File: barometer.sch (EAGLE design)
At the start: 103 parts, among them IC1 TPS5410, IC2 ZPA2326-0311A-R, IC3 MIC5225-3.3v, Q1 BC817, U1 LTC2850, U2 PCA9306, U3 DAC8574, U4 XTR117, U5 XC6215XC6215B182NR, U6 MAX3221, U7 Tiny85-20-SMT, X1 1751248, X2 1751264

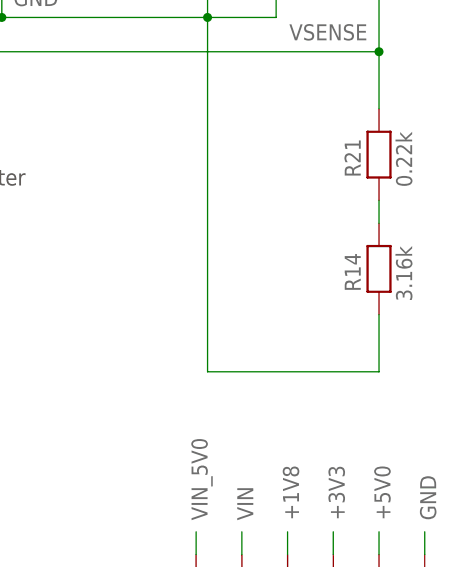
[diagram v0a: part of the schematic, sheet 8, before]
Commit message: Fix feedback resistance in +5V0 buck converter
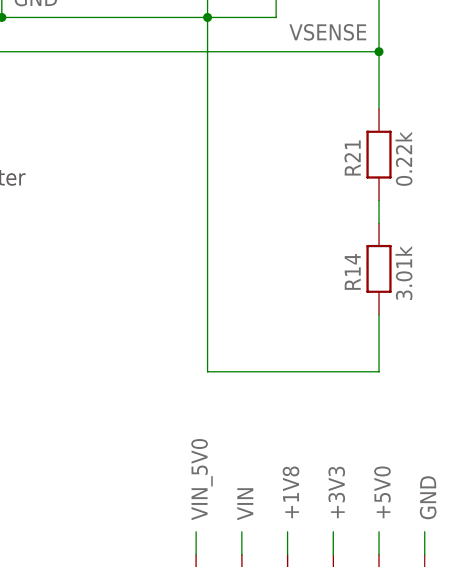
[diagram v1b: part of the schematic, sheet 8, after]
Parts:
- R14: value 3.16k -> 3.01k
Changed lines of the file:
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@@
 <part name="L1" library="inductor-tdk" deviceset="INDUCTOR-TDK" device="VLS6045EX" value="68u"/>
 <part name="R10" library="microbuilder" deviceset="RESISTOR" device="0603" value="10k"/>
-<part name="R14" library="microbuilder" deviceset="RESISTOR" device="0603" value="3.16k"/>
+<part name="R14" library="microbuilder" deviceset="RESISTOR" device="0603" value="3.01k"/>
 <part name="IC2" library="barometer-murata" deviceset="ZPA2326" device="-0311A-R"/>
 <part name="R19" library="microbuilder" deviceset="RESISTOR" device="0603" value="1k"/>

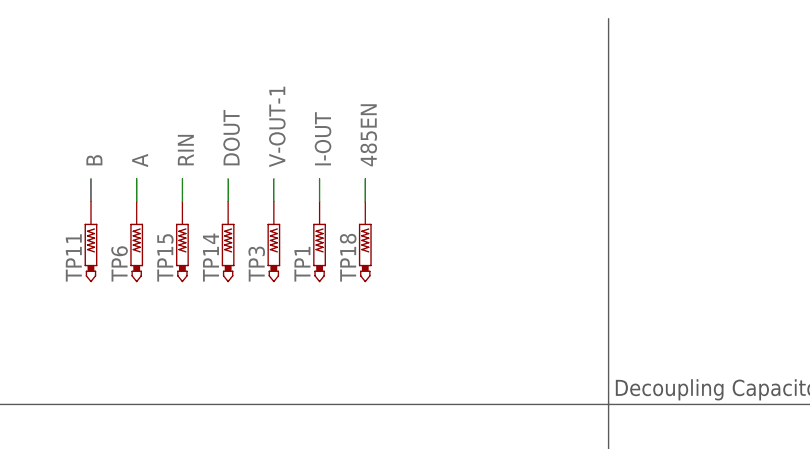
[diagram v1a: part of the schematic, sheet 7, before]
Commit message: Add test point for DAC output corresponding to 4-20 mA current loop
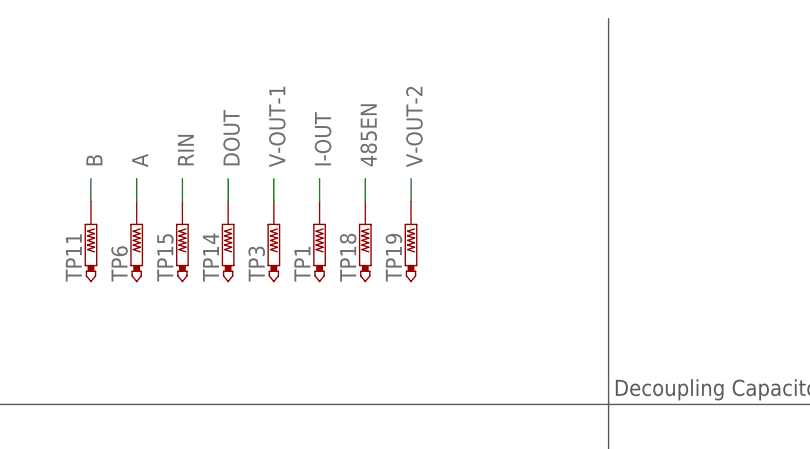
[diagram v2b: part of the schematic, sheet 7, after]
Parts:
- added TP19: PTR1B1,27, testpad:PTR1B1,27
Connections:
- net V-OUT-2: now also TP19.TP
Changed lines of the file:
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@@
 <part name="C19" library="microbuilder" deviceset="CAP_CERAMIC" device="0603" value="0.1u"/>
 <part name="C20" library="microbuilder" deviceset="CAP_CERAMIC" device="0603" value="0.1u"/>
+<part name="TP19" library="testpad" library_urn="urn:adsk.eagle:library:385" deviceset="PTR1" device="B1,27" package3d_urn="urn:adsk.eagle:package:27944/1"/>
 </parts>
 <sheets>
@@
 <attribute name="VALUE" x="143.51" y="152.4" size="1.778" layer="96" font="vector"/>
 </instance>
+<instance part="TP19" gate="G$1" x="66.04" y="152.4" smashed="yes">
+<attribute name="NAME" x="65.024" y="146.05" size="1.778" layer="95" font="vector" rot="R90"/>
+<attribute name="TP_SIGNAL_NAME" x="67.31" y="149.86" size="1.778" layer="97"/>
+</instance>
 </instances>
 <busses>
@@
 <label x="189.865" y="73.66" size="1.778" layer="95" font="vector" rot="R180"/>
 </segment>
-</net>
+<segment>
+<pinref part="TP19" gate="G$1" pin="TP"/>
+<wire x1="66.04" y1="154.94" x2="66.04" y2="157.48" width="0.1524" layer="91"/>
+<label x="67.31" y="158.75" size="1.778" layer="95" font="vector" rot="R90"/>
+</segment>
+</net>

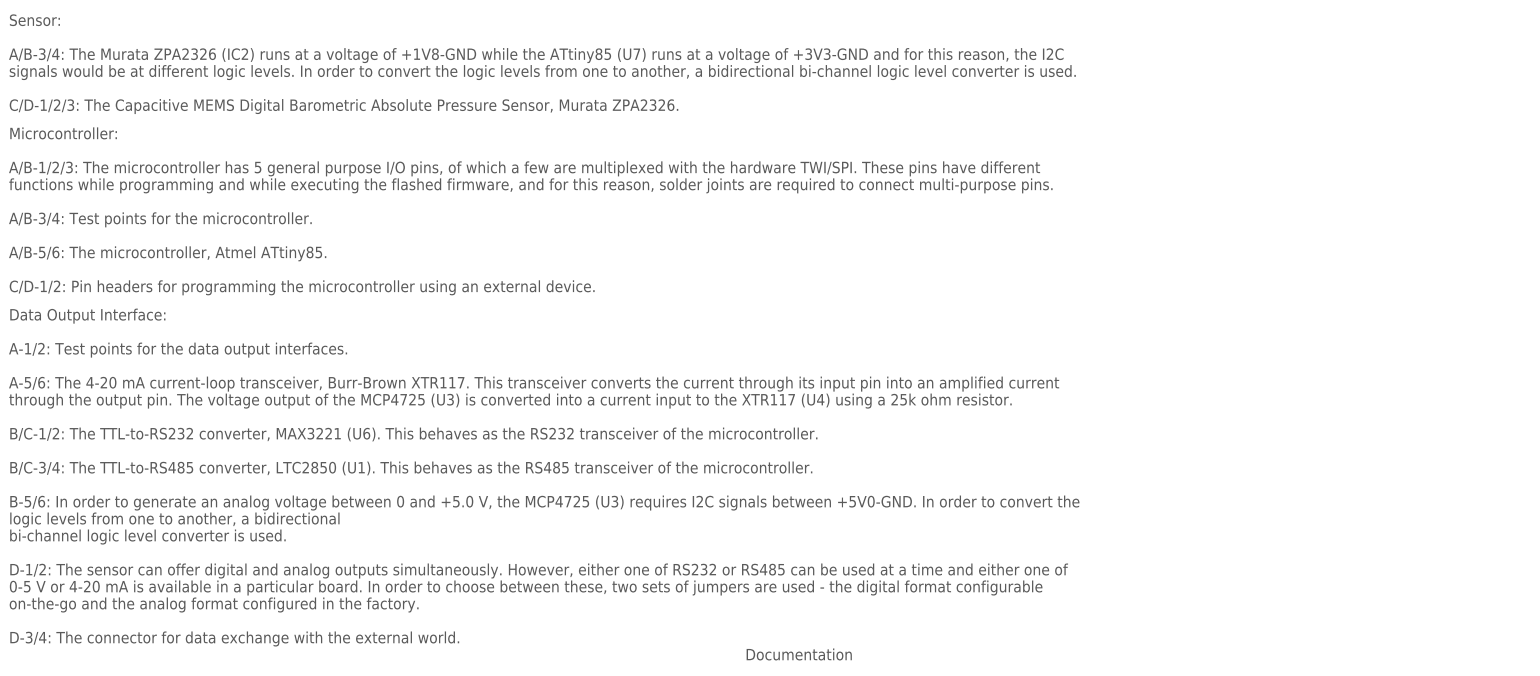
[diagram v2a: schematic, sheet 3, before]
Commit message: Fix schematic documentation
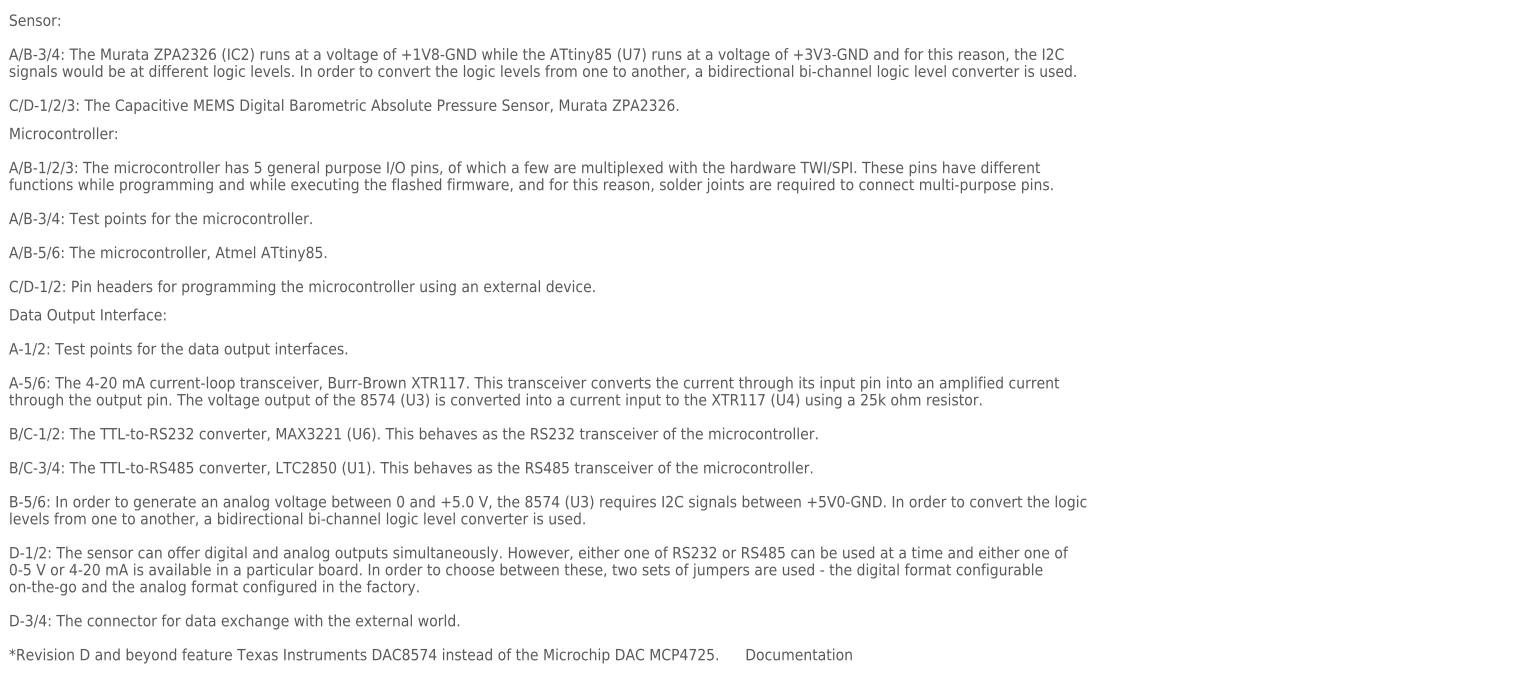
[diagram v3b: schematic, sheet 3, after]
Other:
- note added: "Data Output Interface: A-1/2: Test points for the data output interfaces. A-5/6: The 4-20 mA current-loop transceiver, Burr-Brown XTR117. This transceiver converts the current through its input pin into an amplified current through the output pin. The voltage output of the 8574 (U3) is converted into a current input to the XTR117 (U4) using a 25k ohm resistor. B/C-1/2: The TTL-to-RS232 converter,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"
- note added: "Digital to Analog Converter for 0-5 V terminals 8574"
- note removed: "Data Output Interface: A-1/2: Test points for the data output interfaces. A-5/6: The 4-20 mA current-loop transceiver, Burr-Brown XTR117. This transceiver converts the current through its input pin into an amplified current through the output pin. The voltage output of the MCP4725 (U3) is converted into a current input to the XTR117 (U4) using a 25k ohm resistor. B/C-1/2: The TTL-to-RS232 convert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"
- note removed: "Digital to Analog Converter for 0-5 V terminals MCP4725"
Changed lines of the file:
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@@
 <text x="50.8" y="99.06" size="2.54" layer="97" font="vector" align="center">Digital to Analog Converter
 for 0-5 V terminals
-MCP4725</text>
+8574</text>
 <text x="147.32" y="73.66" size="2.54" layer="97" font="vector" align="center">TTL to RS-232/RS-485
 Transceivers
@@
 A-1/2: Test points for the data output interfaces.
 A-5/6: The 4-20 mA current-loop transceiver, Burr-Brown XTR117. This transceiver converts the current through its input pin into an amplified current
-through the output pin. The voltage output of the MCP4725 (U3) is converted into a current input to the XTR117 (U4) using a 25k ohm resistor.
+through the output pin. The voltage output of the 8574 (U3) is converted into a current input to the XTR117 (U4) using a 25k ohm resistor.
 B/C-1/2: The TTL-to-RS232 converter, MAX3221 (U6). This behaves as the RS232 transceiver of the microcontroller.
 B/C-3/4: The TTL-to-RS485 converter, LTC2850 (U1). This behaves as the RS485 transceiver of the microcontroller.
-B-5/6: In order to generate an analog voltage between 0 and +5.0 V, the MCP4725 (U3) requires I2C signals between +5V0-GND. In order to convert the
-logic levels from one to another, a bidirectional
-bi-channel logic level converter is used.
+B-5/6: In order to generate an analog voltage between 0 and +5.0 V, the 8574 (U3) requires I2C signals between +5V0-GND. In order to convert the logic
+levels from one to another, a bidirectional bi-channel logic level converter is used.
 D-1/2: The sensor can offer digital and analog outputs simultaneously. However, either one of RS232 or RS485 can be used at a time and either one of
 0-5 V or 4-20 mA is available in a particular board. In order to choose between these, two sets of jumpers are used - the digital format configurable
 on-the-go and the analog format configured in the factory.
-D-3/4: The connector for data exchange with the external world.</text>
+D-3/4: The connector for data exchange with the external world.
+*Revision D and beyond feature Texas Instruments DAC8574 instead of the Microchip DAC MCP4725.</text>
 </plain>
 <instances>

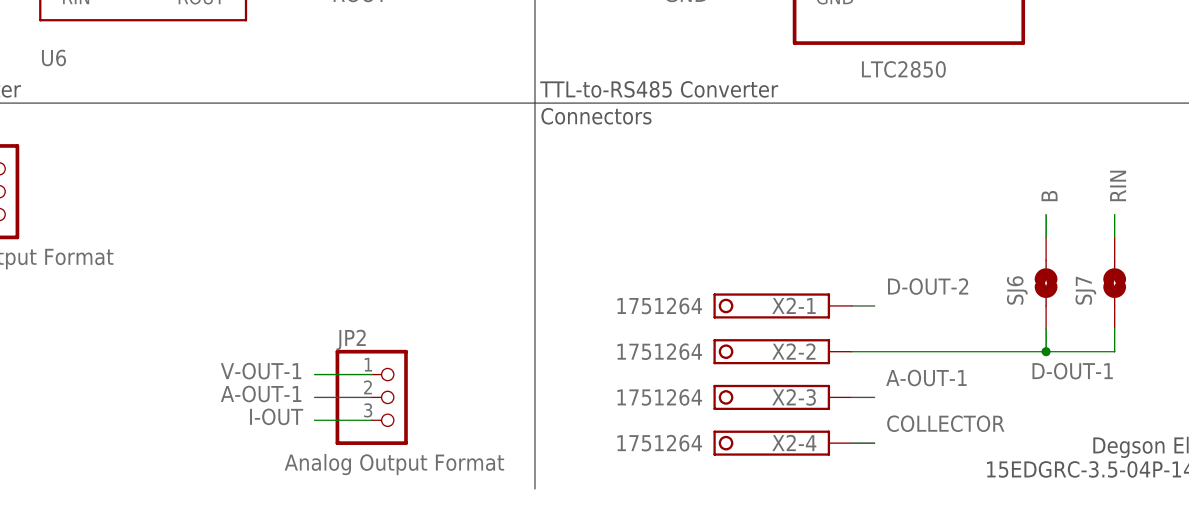
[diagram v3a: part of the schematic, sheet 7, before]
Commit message: Add additional jumper for analog output format
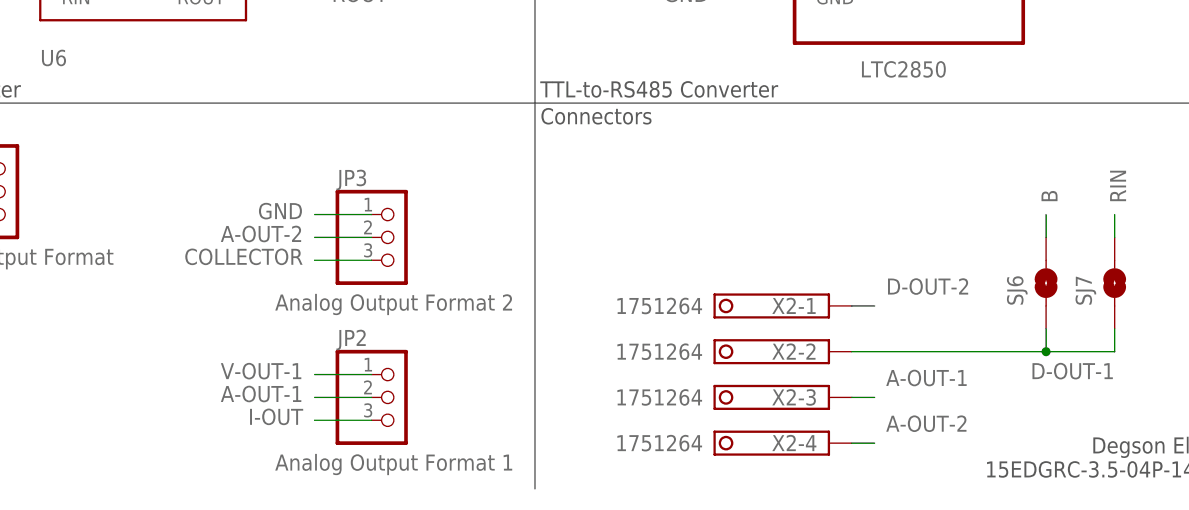
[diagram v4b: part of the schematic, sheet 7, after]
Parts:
- added JP3: Analog Output Format 2, microbuilder:HEADER-1X3SMT
- JP2: value Analog Output Format -> Analog Output Format 1
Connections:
- new net A-OUT-2: JP3.2, X2-4.K
- net COLLECTOR: now also JP3.3; no longer X2-4.K
- net GND: now also JP3.1
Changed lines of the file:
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@@
 <part name="FRAME9" library="microbuilder" deviceset="FRAME_A4_WEATHER" device=""/>
 <part name="R21" library="microbuilder" deviceset="RESISTOR" device="0603" value="0.22k"/>
-<part name="JP2" library="microbuilder" deviceset="HEADER-1X3" device="SMT" value="Analog Output Format"/>
+<part name="JP2" library="microbuilder" deviceset="HEADER-1X3" device="SMT" value="Analog Output Format 1"/>
 <part name="U3" library="texas-msp" deviceset="DAC8574" device=""/>
 <part name="C18" library="microbuilder" deviceset="CAP_CERAMIC" device="0603" value="0.1u"/>
@@
 <part name="C20" library="microbuilder" deviceset="CAP_CERAMIC" device="0603" value="0.1u"/>
 <part name="TP19" library="testpad" library_urn="urn:adsk.eagle:library:385" deviceset="PTR1" device="B1,27" package3d_urn="urn:adsk.eagle:package:27944/1"/>
+<part name="JP3" library="microbuilder" deviceset="HEADER-1X3" device="SMT" value="Analog Output Format 2"/>
 </parts>
 <sheets>
@@
 <attribute name="TP_SIGNAL_NAME" x="67.31" y="149.86" size="1.778" layer="97"/>
 </instance>
+<instance part="JP3" gate="A" x="72.39" y="31.75" smashed="yes">
+<attribute name="NAME" x="66.04" y="37.465" size="1.778" layer="95" font="vector"/>
+<attribute name="VALUE" x="72.39" y="25.4" size="1.778" layer="96" font="vector" align="top-center"/>
+</instance>
 </instances>
 <busses>
@@
 <label x="139.6111" y="145.1356" size="1.778" layer="95" font="vector" rot="MR180"/>
 <pinref part="C20" gate="G$1" pin="P$2"/>
+</segment>
+<segment>
+<pinref part="JP3" gate="A" pin="1"/>
+<wire x1="69.85" y1="34.29" x2="63.5" y2="34.29" width="0.1524" layer="91"/>
+<label x="62.23" y="35.56" size="1.778" layer="95" font="vector" rot="R180"/>
 </segment>
 </net>
@@
 </segment>
 <segment>
-<wire x1="123.19" y1="8.89" x2="125.73" y2="8.89" width="0.1524" layer="91"/>
-<label x="127" y="10.16" size="1.778" layer="95" font="vector"/>
-<pinref part="X2" gate="-4" pin="K"/>
+<pinref part="JP3" gate="A" pin="3"/>
+<wire x1="69.85" y1="29.21" x2="63.5" y2="29.21" width="0.1524" layer="91"/>
+<label x="62.23" y="30.48" size="1.778" layer="95" font="vector" rot="R180"/>
 </segment>
 </net>
@@
 </segment>
 </net>
+<net name="A-OUT-2" class="0">
+<segment>
+<pinref part="JP3" gate="A" pin="2"/>
+<wire x1="69.85" y1="31.75" x2="63.5" y2="31.75" width="0.1524" layer="91"/>
+<label x="62.23" y="33.02" size="1.778" layer="95" font="vector" rot="R180"/>
+</segment>
+<segment>
+<wire x1="123.19" y1="8.89" x2="125.73" y2="8.89" width="0.1524" layer="91"/>
+<label x="127" y="10.16" size="1.778" layer="95" font="vector"/>
+<pinref part="X2" gate="-4" pin="K"/>
+</segment>
+</net>
